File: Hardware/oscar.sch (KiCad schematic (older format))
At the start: 66 parts

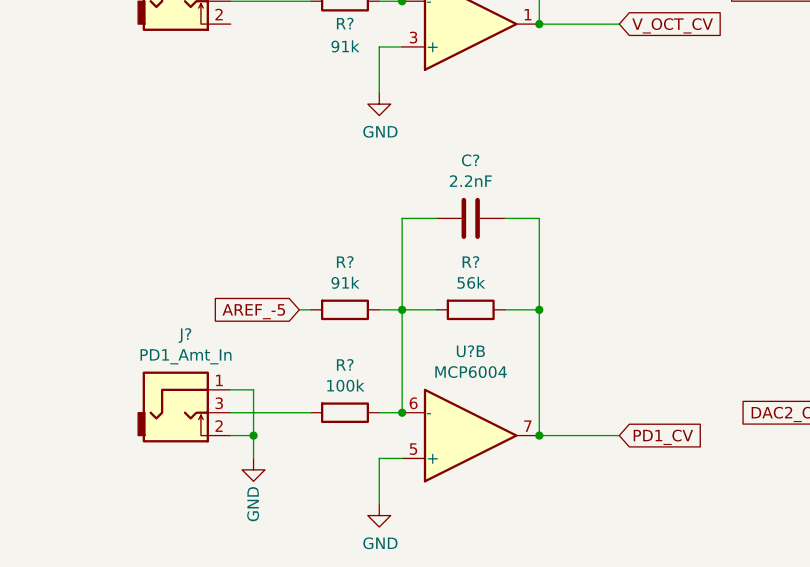
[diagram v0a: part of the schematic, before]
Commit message: Updates to LCD Class
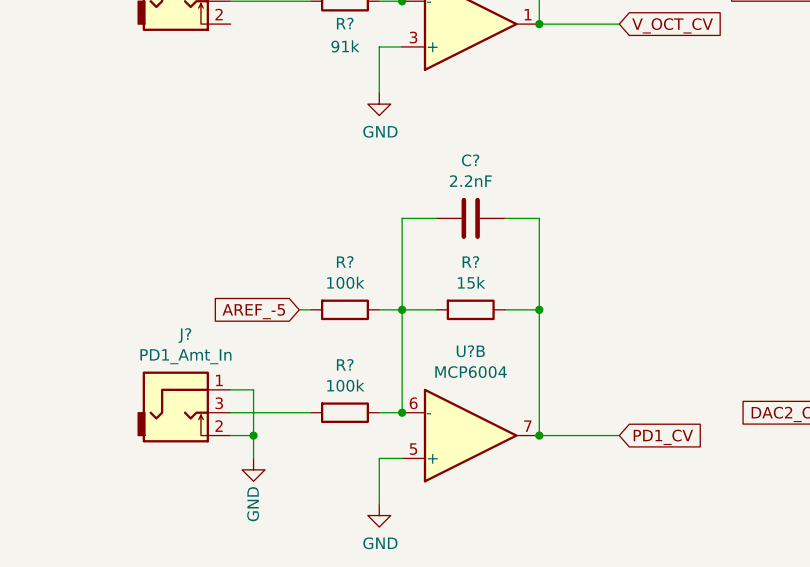
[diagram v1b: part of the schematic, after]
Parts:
- R?: value 56k -> 15k
- R?: value 91k -> 100k
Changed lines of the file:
@@
 EESchema Schematic File Version 4
-LIBS:DisPhaze-cache
+LIBS:oscar-cache
 EELAYER 29 0
 EELAYER END
@@
 P 6050 3400
 F 0 "R?" V 5843 3400 50  0000 C CNN
-F 1 "56k" V 5934 3400 50  0000 C CNN
+F 1 "15k" V 5934 3400 50  0000 C CNN
 F 2 "Resistors_SMD:R_0805_HandSoldering" V 5980 3400 50  0001 C CNN
 F 3 "~" H 6050 3400 50  0001 C CNN
@@
 P 5500 3400
 F 0 "R?" V 5293 3400 50  0000 C CNN
-F 1 "91k" V 5384 3400 50  0000 C CNN
+F 1 "100k" V 5384 3400 50  0000 C CNN
 F 2 "Resistors_SMD:R_0805_HandSoldering" V 5430 3400 50  0001 C CNN
 F 3 "~" H 5500 3400 50  0001 C CNN

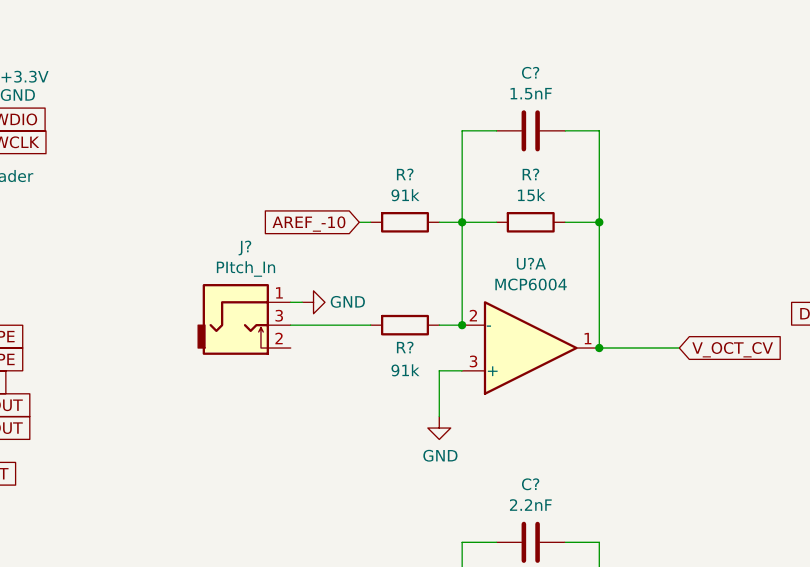
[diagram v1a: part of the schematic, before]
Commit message: Show frequency on oscilloscpe and optimise string drawing
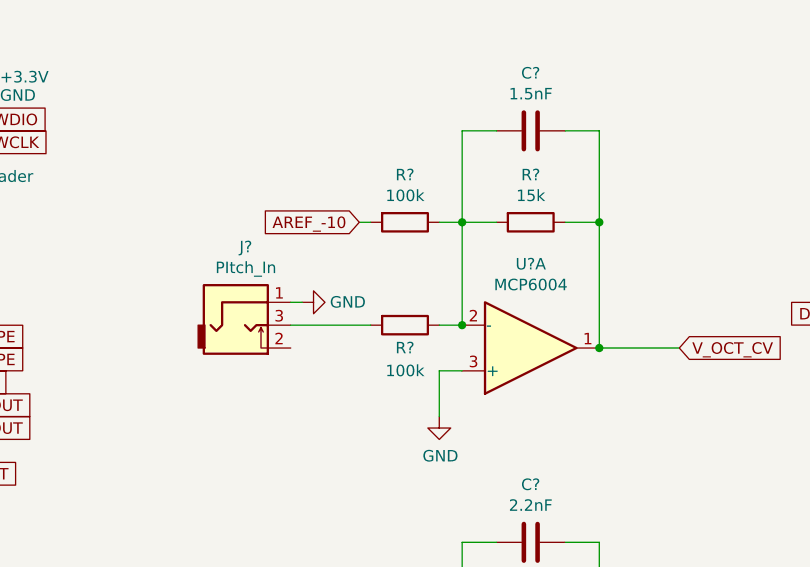
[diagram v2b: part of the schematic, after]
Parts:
- R? (x2): value 91k -> 100k
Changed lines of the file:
@@
 P 5500 1600
 F 0 "R?" V 5293 1600 50  0000 C CNN
-F 1 "91k" V 5384 1600 50  0000 C CNN
+F 1 "100k" V 5384 1600 50  0000 C CNN
 F 2 "Resistors_SMD:R_0805_HandSoldering" V 5430 1600 50  0001 C CNN
 F 3 "~" H 5500 1600 50  0001 C CNN
@@
 P 5500 2050
 F 0 "R?" V 5600 2050 50  0000 C CNN
-F 1 "91k" V 5700 2050 50  0000 C CNN
+F 1 "100k" V 5700 2050 50  0000 C CNN
 F 2 "Resistors_SMD:R_0805_HandSoldering" V 5430 2050 50  0001 C CNN
 F 3 "~" H 5500 2050 50  0001 C CNN

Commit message: Added third channel
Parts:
- removed C?: 1.5nF, Capacitors_SMD:C_0805_HandSoldering, symbol Device:C
- removed R? (x2): 47k, Resistors_SMD:R_0805_HandSoldering, symbol Device:R
- removed R?: 68k, Resistors_SMD:R_0805_HandSoldering, symbol Device:R
- removed R?: 100k, Resistors_SMD:R_0805_HandSoldering, symbol Device:R
- added U?: CR2013-MI2120, Display:CR2013-MI2120, symbol Driver_Display:CR2013-MI2120
- J?: value PItch_In -> ChannelA_In
- J?: value PD1_Amt_In -> ChannelB_In
- J?: value PD2_Amt_In -> ChannelC_In
- J?: value VCA_In -> MIDI_In
- R?: value 47k -> 15k
- R?: value 68k -> 100k
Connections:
- net labels added: AREF_-12, CH_A_OUT, CH_B_OUT, CH_C_OUT, MIDI_OUT
- net labels removed: AREF_-5
- wire segments 219 -> 209
- no-connect marks 39 -> 40
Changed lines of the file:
@@
 $EndComp
 Text GLabel 6700 2150 2    50   Input ~ 0
-V_OCT_CV
+CH_A_OUT
 Wire Wire Line
 	6700 2150 6350 2150
@@
 Connection ~ 11700 5100
 Text GLabel 5300 1600 0    50   Input ~ 0
-AREF_-10
+AREF_-12
 Wire Wire Line
 	5300 1600 5350 1600
@@
 $EndComp
 Text GLabel 6700 3950 2    50   Input ~ 0
-PD1_CV
+CH_B_OUT
 Wire Wire Line
 	6700 3950 6350 3950
@@
 Connection ~ 6350 3400
 Text GLabel 5300 3400 0    50   Input ~ 0
-AREF_-5
+AREF_-12
 Wire Wire Line
 	5300 3400 5350 3400
@@
 P 6050 5300
 F 0 "R?" V 5843 5300 50  0000 C CNN
-F 1 "47k" V 5934 5300 50  0000 C CNN
+F 1 "15k" V 5934 5300 50  0000 C CNN
 F 2 "Resistors_SMD:R_0805_HandSoldering" V 5980 5300 50  0001 C CNN
 F 3 "~" H 6050 5300 50  0001 C CNN
@@
 P 5500 5300
 F 0 "R?" V 5293 5300 50  0000 C CNN
-F 1 "68k" V 5384 5300 50  0000 C CNN
+F 1 "100k" V 5384 5300 50  0000 C CNN
 F 2 "Resistors_SMD:R_0805_HandSoldering" V 5430 5300 50  0001 C CNN
 F 3 "~" H 5500 5300 50  0001 C CNN
@@
 $EndComp
 Text GLabel 6700 5850 2    50   Input ~ 0
-PD2_CV
+CH_C_OUT
 Wire Wire Line
 	6700 5850 6350 5850
@@
 Connection ~ 6350 5300
 Text GLabel 5300 5300 0    50   Input ~ 0
-AREF_-5
+AREF_-12
 Wire Wire Line
 	5300 5300 5350 5300
@@
 F 3 "http://ww1.microchip.com/downloads/en/DeviceDoc/21733j.pdf" H 6100 7950 50  0001 C CNN
 	4    6050 7750
-	1    0    0    1
-$EndComp
-$Comp
-L Device:R R?
-U 1 1 5C8457D0
-P 6050 7200
-F 0 "R?" V 5843 7200 50  0000 C CNN
-F 1 "47k" V 5934 7200 50  0000 C CNN
-F 2 "Resistors_SMD:R_0805_HandSoldering" V 5980 7200 50  0001 C CNN
-F 3 "~" H 6050 7200 50  0001 C CNN
-	1    6050 7200
-	0    1    1    0
-$EndComp
-$Comp
-L Device:R R?
-U 1 1 5C8457D7
-P 5500 7200
-F 0 "R?" V 5293 7200 50  0000 C CNN
-F 1 "68k" V 5384 7200 50  0000 C CNN
-F 2 "Resistors_SMD:R_0805_HandSoldering" V 5430 7200 50  0001 C CNN
-F 3 "~" H 5500 7200 50  0001 C CNN
-	1    5500 7200
-	0    1    1    0
-$EndComp
-$Comp
-L Device:R R?
-U 1 1 5C8457DE
-P 5500 7650
-F 0 "R?" V 5293 7650 50  0000 C CNN
-F 1 "100k" V 5384 7650 50  0000 C CNN
-F 2 "Resistors_SMD:R_0805_HandSoldering" V 5430 7650 50  0001 C CNN
-F 3 "~" H 5500 7650 50  0001 C CNN
-	1    5500 7650
-	0    1    1    0
-$EndComp
-Wire Wire Line
-	6200 7200 6350 7200
-Wire Wire Line
-	6350 7200 6350 7750
-Wire Wire Line
-	5900 7200 5750 7200
-Wire Wire Line
-	5750 7200 5750 7650
-Wire Wire Line
-	5650 7650 5750 7650
-Connection ~ 5750 7650
-Wire Wire Line
-	5650 7200 5750 7200
-Connection ~ 5750 7200
-$Comp
-L power:GND #PWR?
-U 1 1 5C8457ED
-P 5650 8050
-F 0 "#PWR?" H 5650 7800 50  0001 C CNN
-F 1 "GND" H 5655 7877 50  0000 C CNN
-F 2 "" H 5650 8050 50  0001 C CNN
-F 3 "" H 5650 8050 50  0001 C CNN
-	1    5650 8050
-	1    0    0    -1
-$EndComp
-Wire Wire Line
-	5750 7850 5650 7850
-Wire Wire Line
-	5650 7850 5650 8050
-$Comp
-L Device:C C?
-U 1 1 5C8457F5
-P 6050 6800
-F 0 "C?" V 6302 6800 50  0000 C CNN
-F 1 "1.5nF" V 6211 6800 50  0000 C CNN
-F 2 "Capacitors_SMD:C_0805_HandSoldering" H 6088 6650 50  0001 C CNN
-F 3 "~" H 6050 6800 50  0001 C CNN
-	1    6050 6800
-	0    -1   -1   0
+	1    0    0    -1
 $EndComp
 Text GLabel 6700 7750 2    50   Input ~ 0
-VCA
-Wire Wire Line
-	6700 7750 6350 7750
-Connection ~ 6350 7750
-Wire Wire Line
-	5900 6800 5750 6800
-Wire Wire Line
-	5750 6800 5750 7200
-Wire Wire Line
-	6200 6800 6350 6800
-Wire Wire Line
-	6350 6800 6350 7200
-Connection ~ 6350 7200
-Text GLabel 5300 7200 0    50   Input ~ 0
-AREF_-5
-Wire Wire Line
-	5300 7200 5350 7200
+MIDI_OUT
 Text GLabel 1650 3700 0    50   Input ~ 0
 VCA
@@
 P 4800 2050
 F 0 "J?" H 4804 2392 50  0000 C CNN
-F 1 "PItch_In" H 4804 2301 50  0000 C CNN
+F 1 "ChannelA_In" H 4804 2301 50  0000 C CNN
 F 2 "Custom_Footprints:THONKICONN_hole" H 4800 2050 50  0001 C CNN
 F 3 "~" H 4800 2050 50  0001 C CNN
@@
 P 4800 3850
 F 0 "J?" H 4804 4192 50  0000 C CNN
-F 1 "PD1_Amt_In" H 4804 4101 50  0000 C CNN
+F 1 "ChannelB_In" H 4804 4101 50  0000 C CNN
 F 2 "Custom_Footprints:THONKICONN_hole" H 4800 3850 50  0001 C CNN
 F 3 "~" H 4800 3850 50  0001 C CNN
@@
 P 4800 5750
 F 0 "J?" H 4804 6092 50  0000 C CNN
-F 1 "PD2_Amt_In" H 4804 6001 50  0000 C CNN
+F 1 "ChannelC_In" H 4804 6001 50  0000 C CNN
 F 2 "Custom_Footprints:THONKICONN_hole" H 4800 5750 50  0001 C CNN
 F 3 "~" H 4800 5750 50  0001 C CNN
@@
 P 4850 7650
 F 0 "J?" H 4854 7992 50  0000 C CNN
-F 1 "VCA_In" H 4854 7901 50  0000 C CNN
+F 1 "MIDI_In" H 4854 7901 50  0000 C CNN
 F 2 "Custom_Footprints:THONKICONN_hole" H 4850 7650 50  0001 C CNN
 F 3 "~" H 4850 7650 50  0001 C CNN
@@
 	1    0    0    -1
 $EndComp
-$Comp
-L power:GND #PWR?
-U 1 1 5CAEC3B8
-P 5100 7550
-F 0 "#PWR?" H 5100 7300 50  0001 C CNN
-F 1 "GND" V 5100 7350 50  0000 C CNN
-F 2 "" H 5100 7550 50  0001 C CNN
-F 3 "" H 5100 7550 50  0001 C CNN
-	1    5100 7550
-	0    -1   -1   0
-$EndComp
 Wire Wire Line
 	5000 3850 5350 3850
@@
 	5000 5750 5350 5750
 Wire Wire Line
-	5050 7650 5350 7650
-Wire Wire Line
 	5050 7550 5100 7550
-$Comp
-L power:VCC #PWR?
-U 1 1 5CC588A1
-P 5100 8150
-F 0 "#PWR?" H 5100 8000 50  0001 C CNN
-F 1 "VCC" V 5117 8278 50  0000 L CNN
-F 2 "" H 5100 8150 50  0001 C CNN
-F 3 "" H 5100 8150 50  0001 C CNN
-	1    5100 8150
-	-1   0    0    1
-$EndComp
 Text GLabel 1650 3800 0    50   Input ~ 0
 PD2_POT
@@
 Text Notes 8450 800  0    50   ~ 0
 Output Amplifiers
-$Comp
-L Device:R R?
-U 1 1 5CFC5EAE
-P 5100 7950
-F 0 "R?" V 4893 7950 50  0000 C CNN
-F 1 "47k" V 4984 7950 50  0000 C CNN
-F 2 "Resistors_SMD:R_0805_HandSoldering" V 5030 7950 50  0001 C CNN
-F 3 "~" H 5100 7950 50  0001 C CNN
-	1    5100 7950
-	-1   0    0    1
-$EndComp
 Wire Wire Line
 	5050 7750 5100 7750
-Wire Wire Line
-	5100 7750 5100 7800
-Wire Wire Line
-	5100 8100 5100 8150
 NoConn ~ 1850 2000
 NoConn ~ 1850 2200
@@
 	-1   0    0    1
 $EndComp
+NoConn ~ 5100 7550
+Wire Wire Line
+	5050 7650 5750 7650
+Wire Wire Line
+	6350 7750 6500 7750
+Wire Wire Line
+	5750 7850 5550 7850
+Wire Wire Line
+	5550 7850 5550 8300
+Wire Wire Line
+	5550 8300 6500 8300
+Wire Wire Line
+	6500 8300 6500 7750
+Connection ~ 6500 7750
+Wire Wire Line
+	6500 7750 6700 7750
+$Comp
+L Driver_Display:CR2013-MI2120 U?
+U 1 1 5D10A22D
+P 2550 7600
+F 0 "U?" H 2550 8381 50  0000 C CNN
+F 1 "CR2013-MI2120" H 2550 8290 50  0000 C CNN
+F 2 "Display:CR2013-MI2120" H 2550 6900 50  0001 C CNN
+F 3 "http://pan.baidu.com/s/11Y990" H 1900 8100 50  0001 C CNN
+	1    2550 7600
+	1    0    0    -1
+$EndComp
 $EndSCHEMATC

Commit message: First draft of PCB layout
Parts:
- removed C?: 2.2uF, Capacitors_SMD:C_0805_HandSoldering, symbol Device:C
- removed C?: 1.5nF, Capacitors_SMD:C_0805_HandSoldering, symbol Device:C
- removed C?: 100nF, Capacitors_SMD:C_0805_HandSoldering, symbol Device:C
- removed C? (x2): 2.2nF, Capacitors_SMD:C_0805_HandSoldering, symbol Device:C
- removed C? (x2): 10uF, Capacitors_SMD:C_0805_HandSoldering, symbol Device:C
- removed C? (x2): 18pF, Capacitors_SMD:C_0805_HandSoldering, symbol Device:C
- removed D?: LM4040DBZ-10, TO_SOT_Packages_SMD:SOT-23, symbol Reference_Voltage:LM4040DBZ-10
- removed J?: DAC2_Out, Custom_Footprints:THONKICONN_hole, symbol thonkiconn:AudioJack2_Ground_Switch
- removed R?: 2.2k, Resistors_SMD:R_0805_HandSoldering, symbol Device:R
- removed R?: 1k, Resistors_SMD:R_0805_HandSoldering, symbol Device:R
- removed R? (x2): 68k, Resistors_SMD:R_0805_HandSoldering, symbol Device:R
- removed R? (x2): 47k, Resistors_SMD:R_0805_HandSoldering, symbol Device:R
- removed R? (x2): 6.8k, Resistors_SMD:R_0805_HandSoldering, symbol Device:R
- removed U?: STM32F405RGTx, Package_QFP:LQFP-64_10x10mm_P0.5mm, symbol MCU_ST_STM32F4:STM32F405RGTx
- removed U? (x3): TL072, SMD_Packages:SOIC-8-N, symbol Amplifier_Operational:TL072
- removed U?: CR2013-MI2120, Display:CR2013-MI2120, symbol Driver_Display:CR2013-MI2120
- added C10, C16, C8, C9: 100nF, Capacitors_SMD:C_0805_HandSoldering, symbol Device:C
- added C15: 1uF, Capacitors_SMD:CP_Elec_4x5.8, symbol Device:CP
- added J6: ChB_Buff_Out, Custom_Footprints:THONKICONN_hole, symbol thonkiconn:AudioJack2_Ground_Switch
- added J7: ChC_Buff_Out, Custom_Footprints:THONKICONN_hole, symbol thonkiconn:AudioJack2_Ground_Switch
- added R11, R12: 100, Resistors_SMD:R_0805_HandSoldering, symbol Device:R
- added SW1: Left_Encoder, Custom_Footprints:Encoder, symbol Device:Rotary_Encoder_Switch
- added SW2: Right_Encoder, Custom_Footprints:Encoder, symbol Device:Rotary_Encoder_Switch
- added SW3: SW_Push_Dual, Buttons_Switches_SMD:SW_MEC_5GSH9, symbol Switch:SW_Push_Dual
- added U1: STM32F446RETx, Package_QFP:LQFP-64_10x10mm_P0.5mm, symbol MCU_ST_STM32F4:STM32F446RETx
- added U2: ILI9341_SPI, Custom_Footprints:ILI9341_SPI, symbol ili9341_spi:ILI9341_SPI
- added U4: TL074, SMD_Packages:SOIC-14_N, symbol Amplifier_Operational:TL074
- J5: renamed from J?; value DAC1_Out -> ChA_Buff_Out
- R10: renamed from R?; value 1k -> 100
- gave numbers to parts that had none: 32
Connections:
- net labels added: CH_A_IN, CH_B_IN, CH_C_IN, GNDA, LCD_DC, LCD_MOSI, LCD_RESET, LCD_SCK, L_ENC_BTN, L_ENC_DN, L_ENC_UP, NRST, R_ENC_BTN, R_ENC_DN, R_ENC_UP
- net labels removed: AREF_-10, AREF_-12, CH_A_OUT, CH_B_OUT, CH_C_OUT, CTUNE, CV_IN, Calibration, DAC1_OUT, DAC1_RING_MOD, DAC2_MIX, DAC2_OUT, FTUNE, OCTAVE_DN, OCTAVE_UP, PD1_CV, PD1_POT, PD1_TYPE, PD2_CV, PD2_POT, PD2_TYPE, VCA, V_OCT_CV
- wire segments 209 -> 248
- no-connect marks 40 -> 49
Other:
- note removed: "Output Amplifiers"
- moved on the sheet: C11, C14, C2, C3, C5, J2, J3, J4, J5, J8, R1, R10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

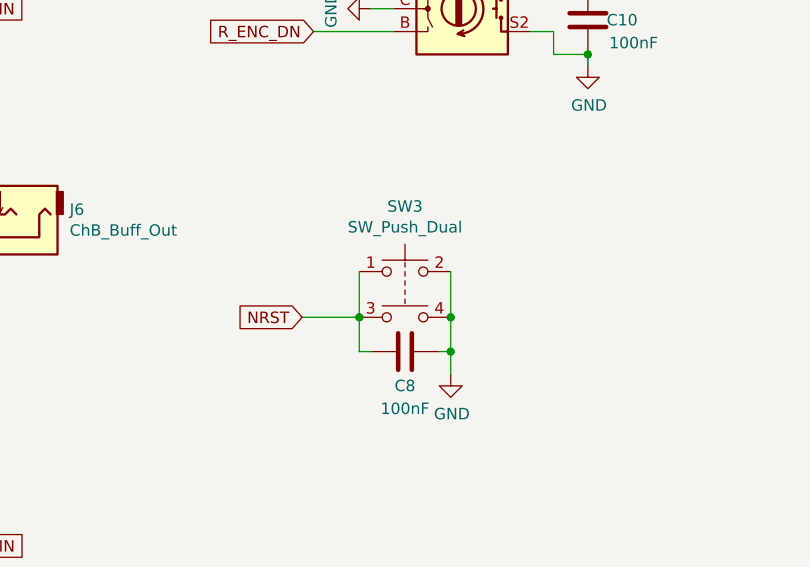
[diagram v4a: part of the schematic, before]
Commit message: Better scaling for horizontal zoom; 4 layer board updates
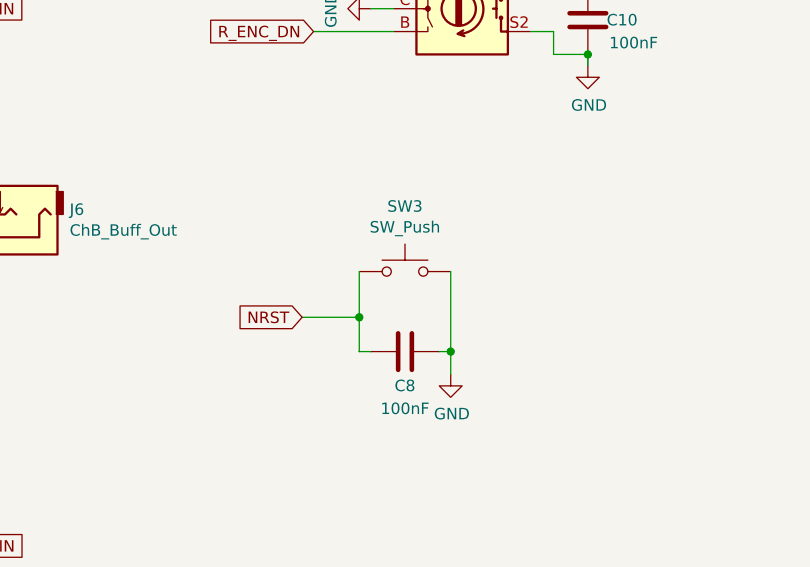
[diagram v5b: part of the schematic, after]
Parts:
- removed SW3: SW_Push_Dual, Buttons_Switches_SMD:SW_MEC_5GSH9, symbol Switch:SW_Push_Dual
- added SW3: SW_Push, Buttons_Switches_THT:SW_PUSH_6mm, symbol Switch:SW_Push
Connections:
- net GND: now also SW3.2
- net NRST: now also SW3.1
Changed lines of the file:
@@
 	9550 3900 9550 3950
 Connection ~ 9550 3900
-$Comp
-L Switch:SW_Push_Dual SW3
-U 1 1 5D769FD2
-P 8750 4850
-F 0 "SW3" H 8750 5135 50  0000 C CNN
-F 1 "SW_Push_Dual" H 8750 5044 50  0000 C CNN
-F 2 "Buttons_Switches_SMD:SW_MEC_5GSH9" H 8750 5050 50  0001 C CNN
-F 3 "~" H 8750 5050 50  0001 C CNN
-	1    8750 4850
-	1    0    0    -1
-$EndComp
 Wire Wire Line
 	8550 4850 8550 5050
-Wire Wire Line
-	8950 4850 8950 5050
-Wire Wire Line
-	8950 5050 8950 5200
-Connection ~ 8950 5050
 $Comp
 L Device:C C8
@@
 	-1   0    0    1
 $EndComp
+$Comp
+L Switch:SW_Push SW3
+U 1 1 5D32F73D
+P 8750 4850
+F 0 "SW3" H 8750 5135 50  0000 C CNN
+F 1 "SW_Push" H 8750 5044 50  0000 C CNN
+F 2 "Buttons_Switches_THT:SW_PUSH_6mm" H 8750 5050 50  0001 C CNN
+F 3 "~" H 8750 5050 50  0001 C CNN
+	1    8750 4850
+	1    0    0    -1
+$EndComp
+Wire Wire Line
+	8950 4850 8950 5200
 $EndSCHEMATC
